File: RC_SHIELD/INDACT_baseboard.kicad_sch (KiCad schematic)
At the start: 1 part

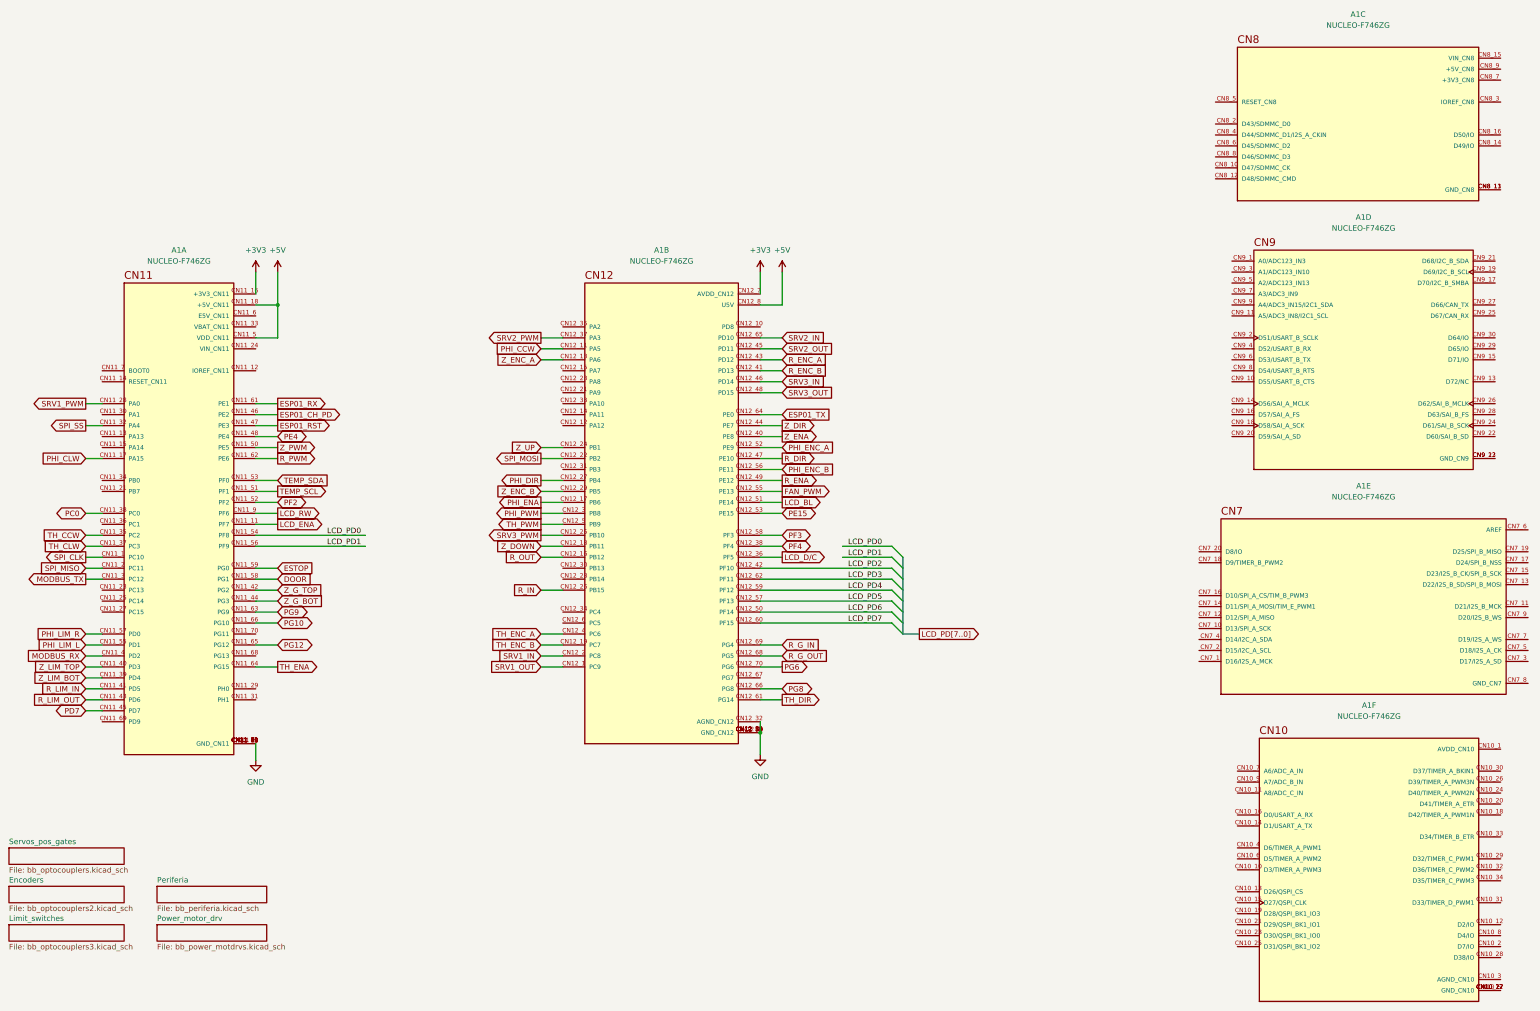
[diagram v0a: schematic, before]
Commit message: added secondary MCU to schematic and made it more consistent
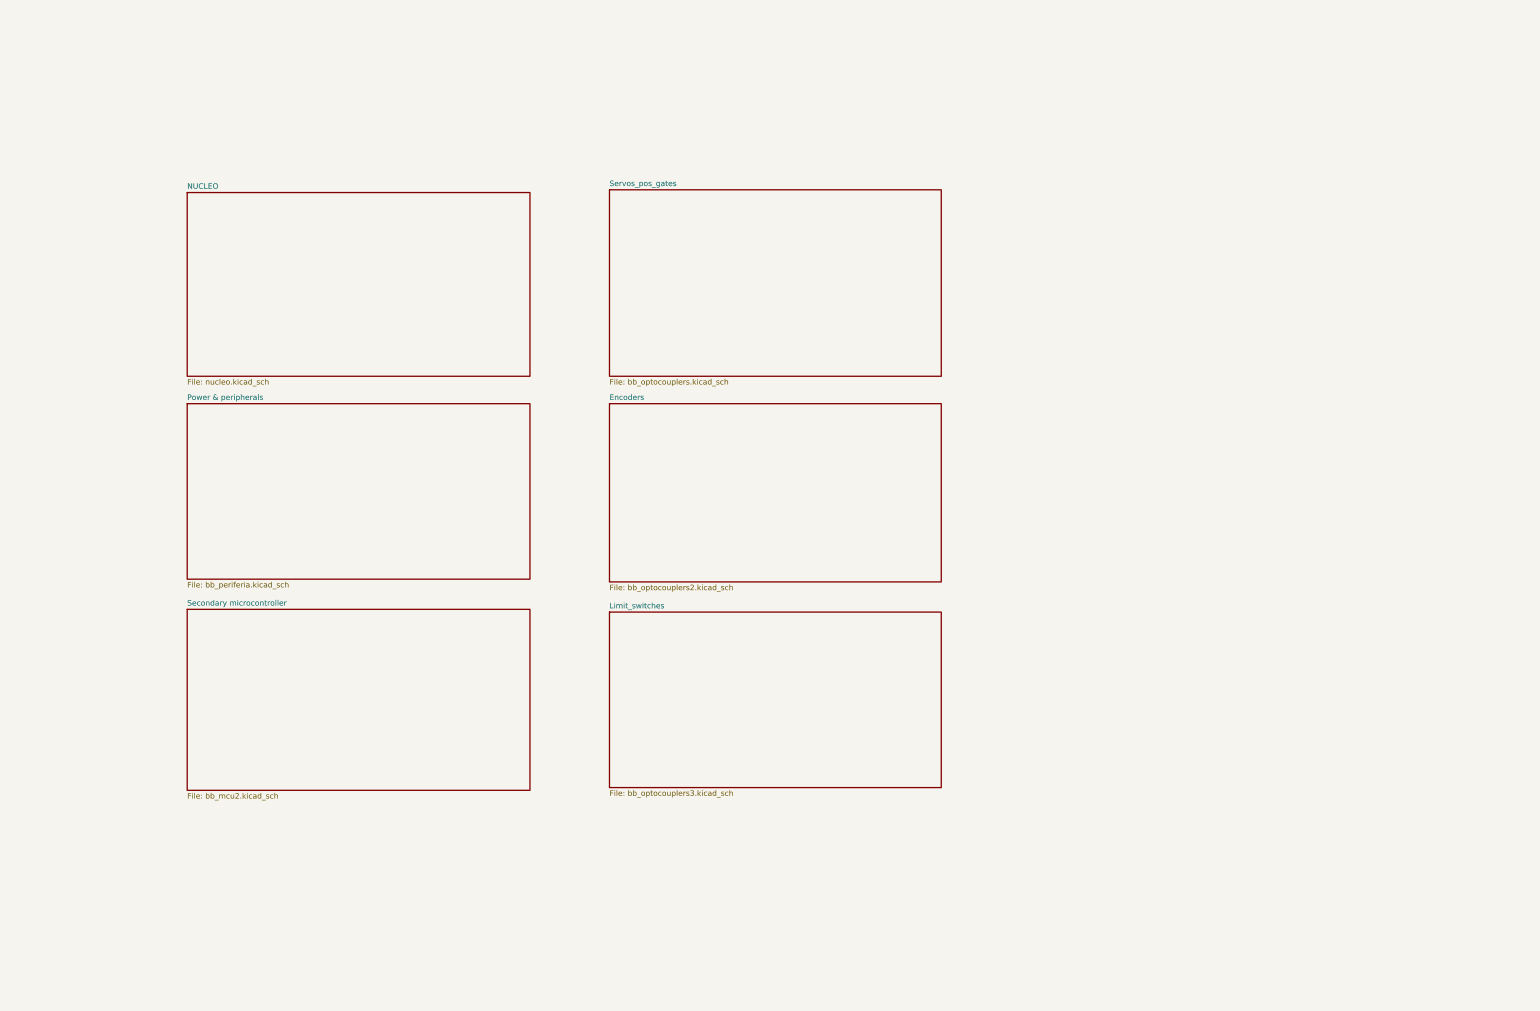
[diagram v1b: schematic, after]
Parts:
- removed A1: NUCLEO-F746ZG, NUCLEO-F746ZG:MODULE_NUCLEO-F746ZG, symbol NUCLEO-F746ZG:NUCLEO-F746ZG
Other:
- sheet Periferia renamed Power & peripherals
- sheet Power_motor_drv renamed Secondary microcontroller
- added sheet NUCLEO (nucleo.kicad_sch)
- sheet Secondary microcontroller: file bb_power_motdrvs.kicad_sch -> bb_mcu2.kicad_sch
- company: (none) -> LEGO Kör (legokor.hu)
- title: NUCLEO -> Karcsi (INDACT Robot Arm)

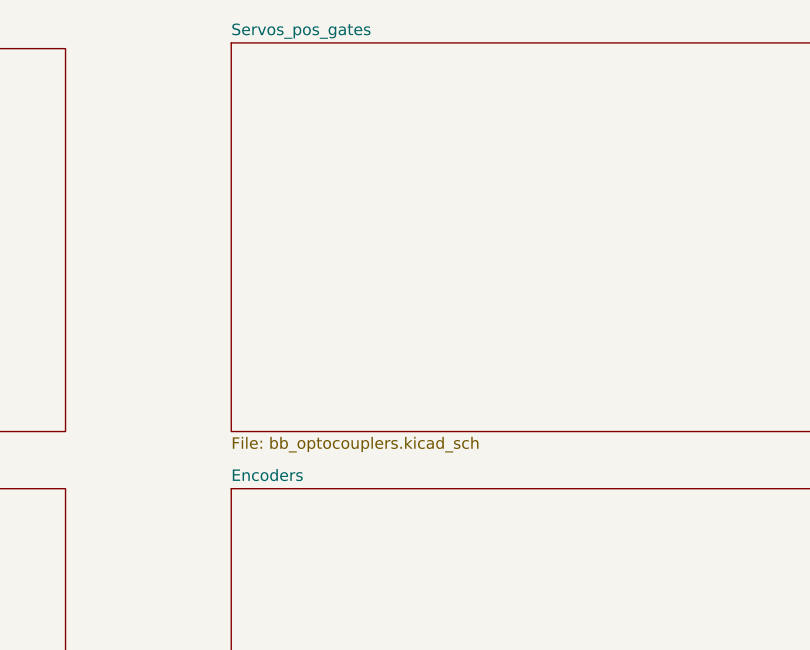
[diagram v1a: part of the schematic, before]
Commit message: [SCH] reorganized optocouplers and tidied up page 2
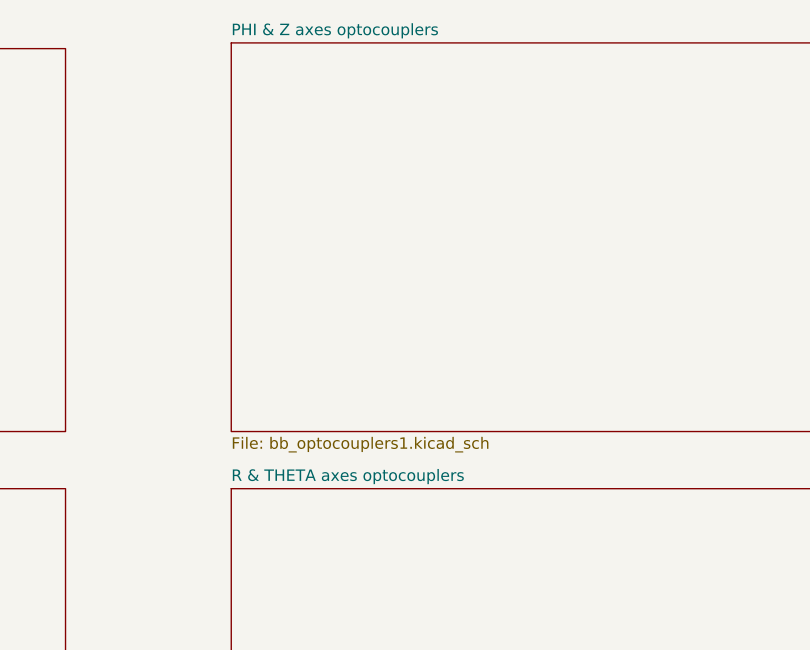
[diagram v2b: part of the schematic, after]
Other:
- sheet Encoders renamed R & THETA axes optocouplers
- sheet Servos_pos_gates renamed PHI & Z axes optocouplers
- sheet PHI & Z axes optocouplers: file bb_optocouplers.kicad_sch -> bb_optocouplers1.kicad_sch
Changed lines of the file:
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@@
     (stroke (width 0.1524) (type solid))
     (fill (color 0 0 0 0.0000))
-    (property "Sheetname" "Encoders" (at 160.655 69.1384 0)
+    (property "Sheetname" "R & THETA axes optocouplers" (at 160.655 69.1384 0)
       (effects (font (size 1.27 1.27)) (justify left bottom))
     )
@@
     (stroke (width 0.1524) (type solid))
     (fill (color 0 0 0 0.0000))
-    (property "Sheetname" "Servos_pos_gates" (at 160.655 19.6084 0)
+    (property "Sheetname" "PHI & Z axes optocouplers" (at 160.655 19.6084 0)
       (effects (font (size 1.27 1.27)) (justify left bottom))
     )
-    (property "Sheetfile" "bb_optocouplers.kicad_sch" (at 160.655 64.0846 0)
+    (property "Sheetfile" "bb_optocouplers1.kicad_sch" (at 160.655 64.0846 0)
       (effects (font (size 1.27 1.27)) (justify left top))
     )

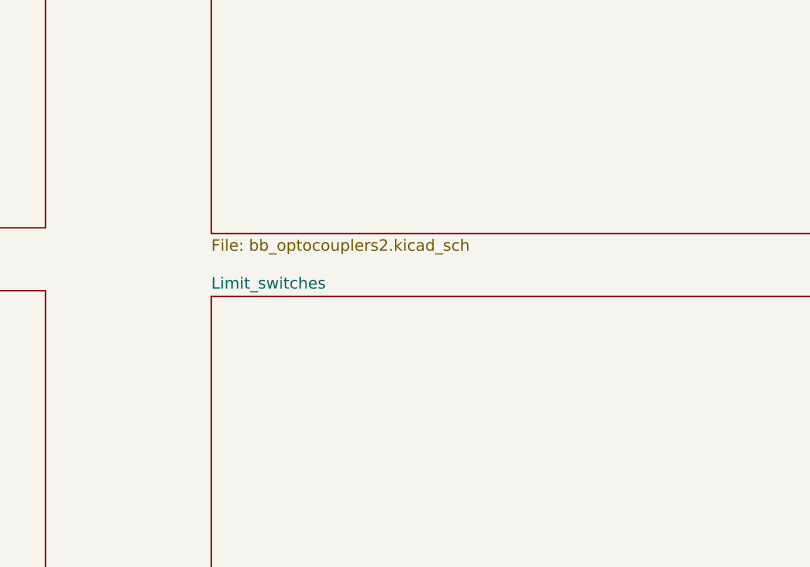
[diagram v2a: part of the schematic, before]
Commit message: [SCH] added "exclude from BOM" signs
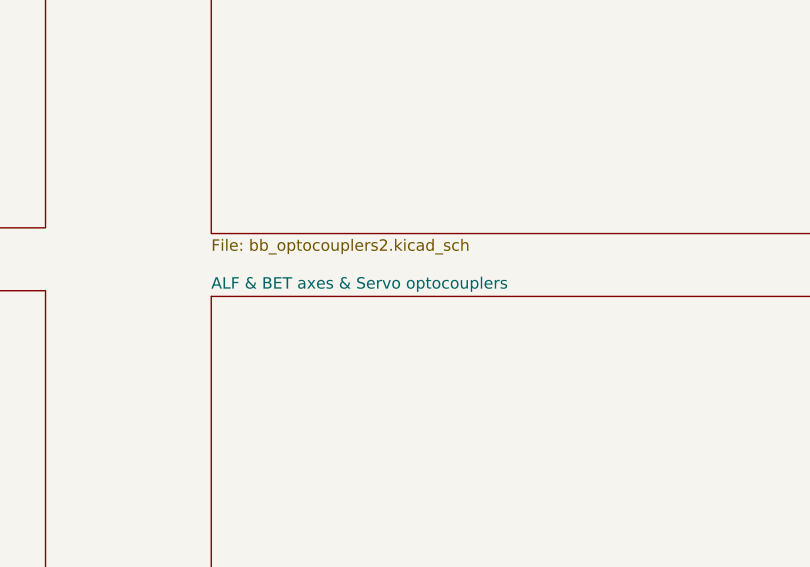
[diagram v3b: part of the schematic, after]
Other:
- sheet Limit_switches renamed ALF & BET axes & Servo optocouplers
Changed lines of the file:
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@@
     (stroke (width 0.1524) (type solid))
     (fill (color 0 0 0 0.0000))
-    (property "Sheetname" "Limit_switches" (at 160.655 117.3984 0)
+    (property "Sheetname" "ALF & BET axes & Servo optocouplers" (at 160.655 117.3984 0)
       (effects (font (size 1.27 1.27)) (justify left bottom))
     )

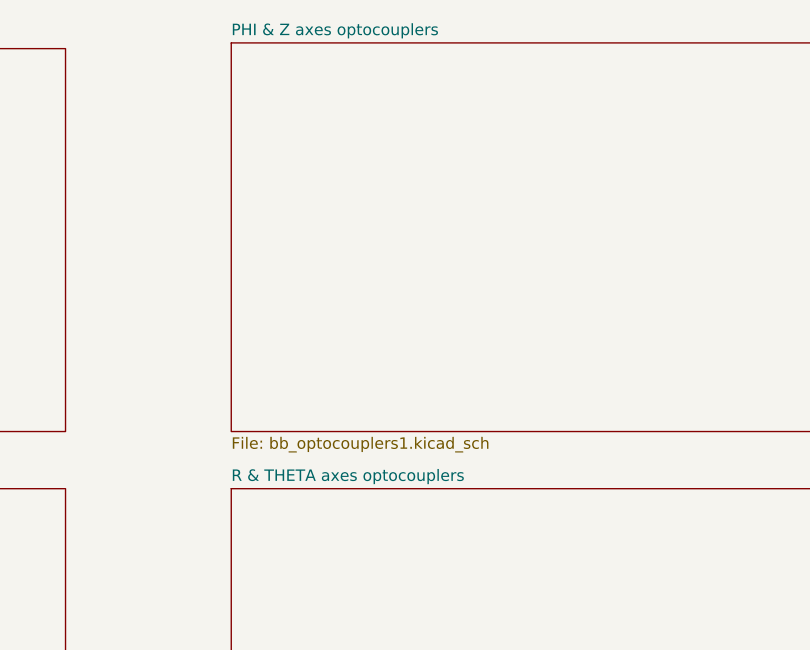
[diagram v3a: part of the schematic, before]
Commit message: Revert "[SCH] reorganized optocouplers and tidied up page 2"
This reverts commit 005640e4067293c5014d1b79d289b32d97da3ff9.
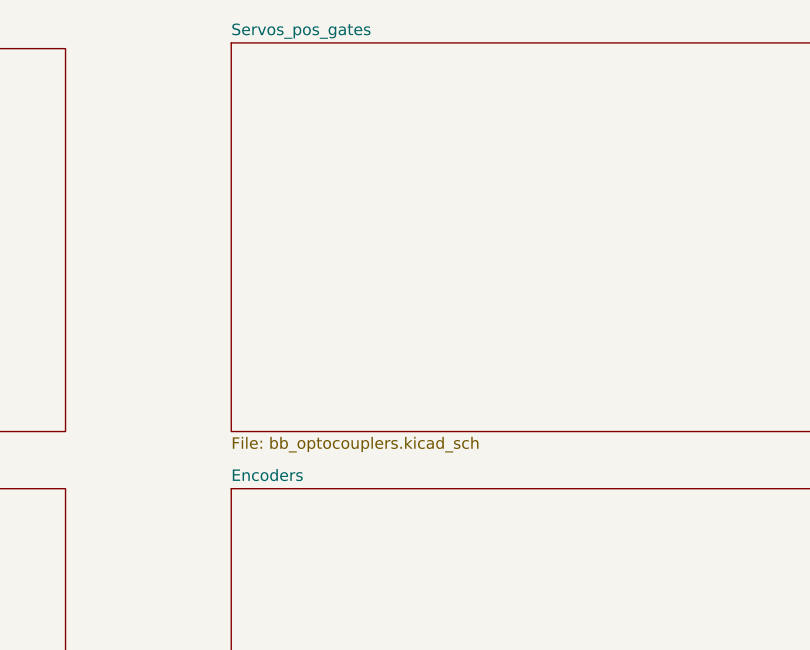
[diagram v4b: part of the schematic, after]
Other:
- sheet PHI & Z axes optocouplers renamed Servos_pos_gates
- sheet R & THETA axes optocouplers renamed Encoders
- sheet Servos_pos_gates: file bb_optocouplers1.kicad_sch -> bb_optocouplers.kicad_sch
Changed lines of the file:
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@@
     (stroke (width 0.1524) (type solid))
     (fill (color 0 0 0 0.0000))
-    (property "Sheetname" "R & THETA axes optocouplers" (at 160.655 69.1384 0)
+    (property "Sheetname" "Encoders" (at 160.655 69.1384 0)
       (effects (font (size 1.27 1.27)) (justify left bottom))
     )
@@
     (stroke (width 0.1524) (type solid))
     (fill (color 0 0 0 0.0000))
-    (property "Sheetname" "PHI & Z axes optocouplers" (at 160.655 19.6084 0)
+    (property "Sheetname" "Servos_pos_gates" (at 160.655 19.6084 0)
       (effects (font (size 1.27 1.27)) (justify left bottom))
     )
-    (property "Sheetfile" "bb_optocouplers1.kicad_sch" (at 160.655 64.0846 0)
+    (property "Sheetfile" "bb_optocouplers.kicad_sch" (at 160.655 64.0846 0)
       (effects (font (size 1.27 1.27)) (justify left top))
     )

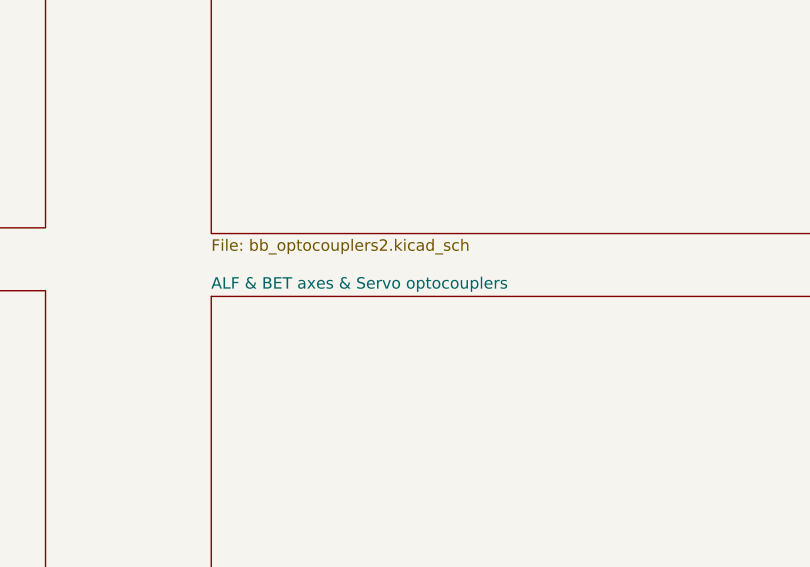
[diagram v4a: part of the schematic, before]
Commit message: [SCH] fixed Nucleo papercuts
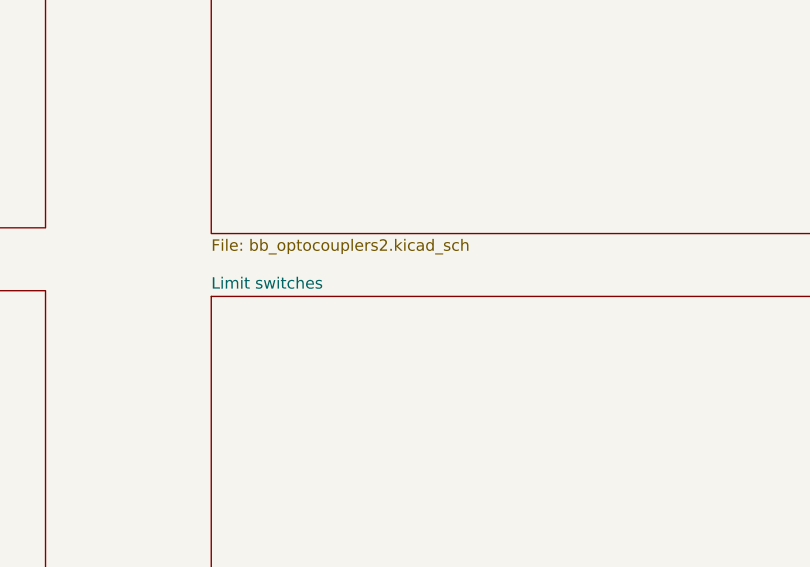
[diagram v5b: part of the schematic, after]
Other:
- sheet ALF & BET axes & Servo optocouplers renamed Limit switches
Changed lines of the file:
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@@
     (stroke (width 0.1524) (type solid))
     (fill (color 0 0 0 0.0000))
-    (property "Sheetname" "ALF & BET axes & Servo optocouplers" (at 160.655 117.3984 0)
+    (property "Sheetname" "Limit switches" (at 160.655 117.3984 0)
       (effects (font (size 1.27 1.27)) (justify left bottom))
     )
